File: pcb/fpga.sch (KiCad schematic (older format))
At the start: 29 parts, among them J1 CONN_INTEGRALSTICK_FPGA_DEVICE, Q1 SSM6N58NU, Q2 SSM6N58NU, Q3 SSM6N58NU, U12 DSC6001HI2A-025.0000‎, U2 XC7A50T-1FTG256C, U9 AT24MAC402-UDFN

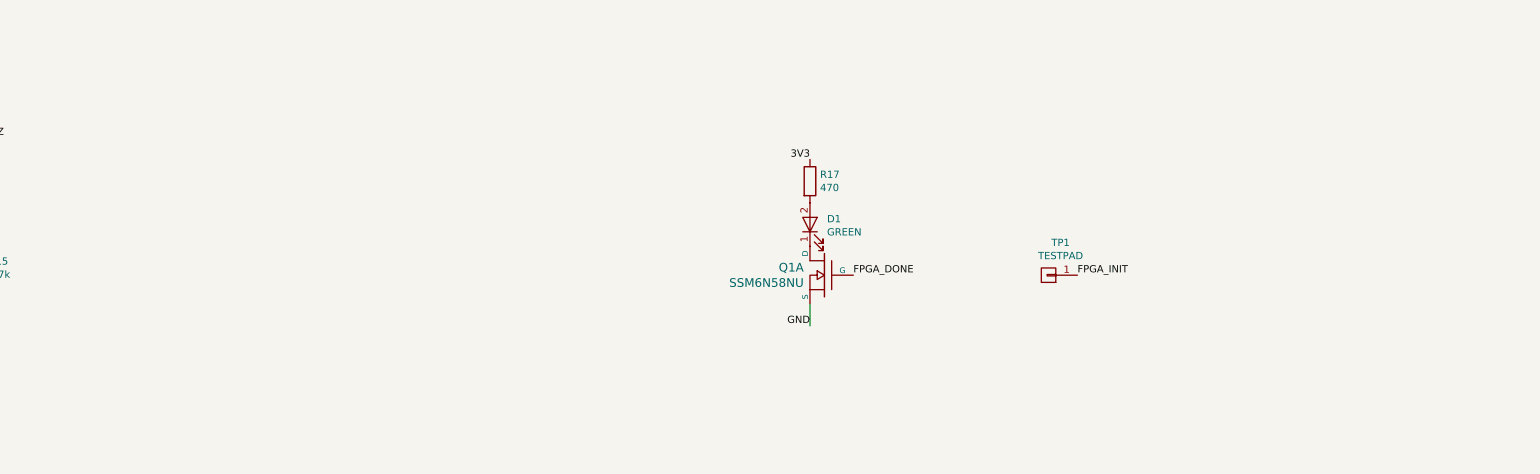
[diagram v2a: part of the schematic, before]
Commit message: Added layer-change caps by Q-strip
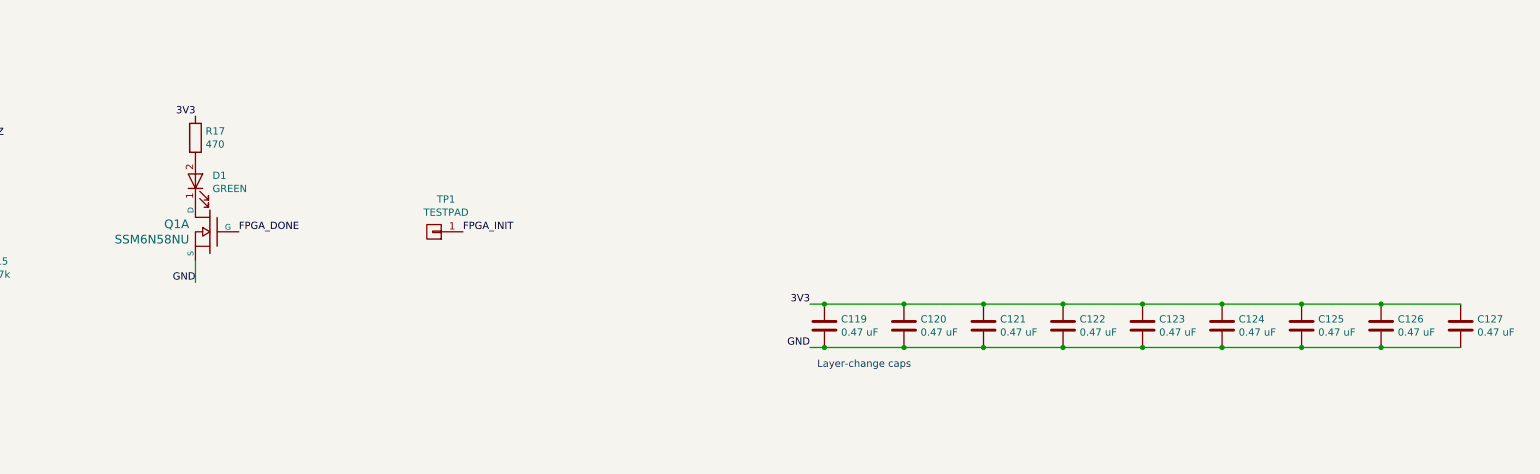
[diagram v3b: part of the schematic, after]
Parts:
- added C119, C120, C121, C122, C123, C124, C125, C126, C127: 0.47 uF, azonenberg_pcb:EIA_0402_CAP_NOSILK, symbol device:C
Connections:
- net 3V3: now also C119.1, C120.1, C121.1, C122.1, C123.1, C124.1, C125.1, C126.1, C127.1
- net GND: now also C119.2, C120.2, C121.2, C122.2, C123.2, C124.2, C125.2, C126.2, C127.2
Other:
- note added: "Layer-change caps"
- moved on the sheet: D1, Q1A, R17, TP1
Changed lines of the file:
@@
 Sheet 6 8
 Title "INTEGRALSTICK Compute Module"
-Date "2018-11-12"
+Date "2018-11-13"
 Rev "0.1"
 Comp "Andrew D. Zonenberg"
@@
 L special-azonenberg:SSM6N58NU_DUAL_NMOS Q1
 U 1 1 5BF27F1F
-P 11200 8050
-F 0 "Q1" H 11343 8103 60  0000 L CNN
-F 1 "SSM6N58NU" H 11343 7997 60  0000 L CNN
-F 2 "azonenberg_pcb:DFN_6_0.65MM_2x2MM_GDS" H 11200 8050 60  0001 C CNN
-F 3 "" H 11343 7944 60  0000 L CNN
-	1    11200 8050
+P 6950 7750
+F 0 "Q1" H 7093 7803 60  0000 L CNN
+F 1 "SSM6N58NU" H 7093 7697 60  0000 L CNN
+F 2 "azonenberg_pcb:DFN_6_0.65MM_2x2MM_GDS" H 6950 7750 60  0001 C CNN
+F 3 "" H 7093 7644 60  0000 L CNN
+	1    6950 7750
 	-1   0    0    -1
 $EndComp
@@
 L device:LED D1
 U 1 1 5BF295E2
-P 11100 7700
-F 0 "D1" V 11139 7582 50  0000 R CNN
-F 1 "GREEN" V 11048 7582 50  0000 R CNN
-F 2 "azonenberg_pcb:EIA_0603_LED" H 11100 7700 50  0001 C CNN
-F 3 "" H 11100 7700 50  0001 C CNN
-	1    11100 7700
+P 6850 7400
+F 0 "D1" V 6889 7282 50  0000 R CNN
+F 1 "GREEN" V 6798 7282 50  0000 R CNN
+F 2 "azonenberg_pcb:EIA_0603_LED" H 6850 7400 50  0001 C CNN
+F 3 "" H 6850 7400 50  0001 C CNN
+	1    6850 7400
 	0    -1   -1   0
 $EndComp
@@
 L device:R R17
 U 1 1 5BF2B413
-P 11100 7400
-F 0 "R17" H 11170 7446 50  0000 L CNN
-F 1 "470" H 11170 7355 50  0000 L CNN
-F 2 "azonenberg_pcb:EIA_0402_RES_NOSILK" V 11030 7400 50  0001 C CNN
-F 3 "" H 11100 7400 50  0001 C CNN
-	1    11100 7400
-	1    0    0    -1
-$EndComp
-Text Label 11100 7250 2    50   ~ 0
+P 6850 7100
+F 0 "R17" H 6920 7146 50  0000 L CNN
+F 1 "470" H 6920 7055 50  0000 L CNN
+F 2 "azonenberg_pcb:EIA_0402_RES_NOSILK" V 6780 7100 50  0001 C CNN
+F 3 "" H 6850 7100 50  0001 C CNN
+	1    6850 7100
+	1    0    0    -1
+$EndComp
+Text Label 6850 6950 2    50   ~ 0
 3V3
-Text Label 11100 8400 2    50   ~ 0
-GND
-Text Label 11400 8050 0    50   ~ 0
+Text Label 6850 8100 2    50   ~ 0
+GND
+Text Label 7150 7750 0    50   ~ 0
 FPGA_DONE
-Text Label 12950 8050 0    50   ~ 0
+Text Label 8700 7750 0    50   ~ 0
 FPGA_INIT
 Text Label 13750 5050 2    50   ~ 0
@@
 Connection ~ 12850 5050
 Wire Wire Line
-	11100 8250 11100 8400
+	6850 7950 6850 8100
 $Comp
 L conn:CONN_01X01 TP1
 U 1 1 5BF366F5
-P 12750 8050
-F 0 "TP1" H 12667 7825 50  0000 C CNN
-F 1 "TESTPAD" H 12667 7916 50  0000 C CNN
-F 2 "azonenberg_pcb:TESTPOINT_SMT_0.5MM" H 12750 8050 50  0001 C CNN
-F 3 "" H 12750 8050 50  0001 C CNN
-	1    12750 8050
+P 8500 7750
+F 0 "TP1" H 8417 7525 50  0000 C CNN
+F 1 "TESTPAD" H 8417 7616 50  0000 C CNN
+F 2 "azonenberg_pcb:TESTPOINT_SMT_0.5MM" H 8500 7750 50  0001 C CNN
+F 3 "" H 8500 7750 50  0001 C CNN
+	1    8500 7750
 	-1   0    0    1
 $EndComp
@@
 NoConn ~ 8400 4550
 NoConn ~ 8400 4450
+Text Notes 11150 8700 0    50   ~ 0
+Layer-change caps
+$Comp
+L device:C C?
+U 1 1 5BFC1C0D
+P 11200 8400
+AR Path="/5B6B7044/5BFC1C0D" Ref="C?"  Part="1"
+AR Path="/5B6B702C/5BFC1C0D" Ref="C119"  Part="1"
+F 0 "C119" H 11315 8446 50  0000 L CNN
+F 1 "0.47 uF" H 11315 8355 50  0000 L CNN
+F 2 "azonenberg_pcb:EIA_0402_CAP_NOSILK" H 11238 8250 50  0001 C CNN
+F 3 "" H 11200 8400 50  0001 C CNN
+	1    11200 8400
+	1    0    0    -1
+$EndComp
+Text Label 11100 8250 2    50   ~ 0
+3V3
+Text Label 11100 8550 2    50   ~ 0
+GND
+$Comp
+L device:C C?
+U 1 1 5BFC3321
+P 12300 8400
+AR Path="/5B6B7044/5BFC3321" Ref="C?"  Part="1"
+AR Path="/5B6B702C/5BFC3321" Ref="C121"  Part="1"
+F 0 "C121" H 12415 8446 50  0000 L CNN
+F 1 "0.47 uF" H 12415 8355 50  0000 L CNN
+F 2 "azonenberg_pcb:EIA_0402_CAP_NOSILK" H 12338 8250 50  0001 C CNN
+F 3 "" H 12300 8400 50  0001 C CNN
+	1    12300 8400
+	1    0    0    -1
+$EndComp
+$Comp
+L device:C C?
+U 1 1 5BFC390F
+P 12850 8400
+AR Path="/5B6B7044/5BFC390F" Ref="C?"  Part="1"
+AR Path="/5B6B702C/5BFC390F" Ref="C122"  Part="1"
+F 0 "C122" H 12965 8446 50  0000 L CNN
+F 1 "0.47 uF" H 12965 8355 50  0000 L CNN
+F 2 "azonenberg_pcb:EIA_0402_CAP_NOSILK" H 12888 8250 50  0001 C CNN
+F 3 "" H 12850 8400 50  0001 C CNN
+	1    12850 8400
+	1    0    0    -1
+$EndComp
+$Comp
+L device:C C?
+U 1 1 5BFC3D49
+P 13400 8400
+AR Path="/5B6B7044/5BFC3D49" Ref="C?"  Part="1"
+AR Path="/5B6B702C/5BFC3D49" Ref="C123"  Part="1"
+F 0 "C123" H 13515 8446 50  0000 L CNN
+F 1 "0.47 uF" H 13515 8355 50  0000 L CNN
+F 2 "azonenberg_pcb:EIA_0402_CAP_NOSILK" H 13438 8250 50  0001 C CNN
+F 3 "" H 13400 8400 50  0001 C CNN
+	1    13400 8400
+	1    0    0    -1
+$EndComp
+$Comp
+L device:C C?
+U 1 1 5BFC4329
+P 13950 8400
+AR Path="/5B6B7044/5BFC4329" Ref="C?"  Part="1"
+AR Path="/5B6B702C/5BFC4329" Ref="C124"  Part="1"
+F 0 "C124" H 14065 8446 50  0000 L CNN
+F 1 "0.47 uF" H 14065 8355 50  0000 L CNN
+F 2 "azonenberg_pcb:EIA_0402_CAP_NOSILK" H 13988 8250 50  0001 C CNN
+F 3 "" H 13950 8400 50  0001 C CNN
+	1    13950 8400
+	1    0    0    -1
+$EndComp
+$Comp
+L device:C C?
+U 1 1 5BFC4780
+P 14500 8400
+AR Path="/5B6B7044/5BFC4780" Ref="C?"  Part="1"
+AR Path="/5B6B702C/5BFC4780" Ref="C125"  Part="1"
+F 0 "C125" H 14615 8446 50  0000 L CNN
+F 1 "0.47 uF" H 14615 8355 50  0000 L CNN
+F 2 "azonenberg_pcb:EIA_0402_CAP_NOSILK" H 14538 8250 50  0001 C CNN
+F 3 "" H 14500 8400 50  0001 C CNN
+	1    14500 8400
+	1    0    0    -1
+$EndComp
+$Comp
+L device:C C?
+U 1 1 5BFC4BF1
+P 15050 8400
+AR Path="/5B6B7044/5BFC4BF1" Ref="C?"  Part="1"
+AR Path="/5B6B702C/5BFC4BF1" Ref="C126"  Part="1"
+F 0 "C126" H 15165 8446 50  0000 L CNN
+F 1 "0.47 uF" H 15165 8355 50  0000 L CNN
+F 2 "azonenberg_pcb:EIA_0402_CAP_NOSILK" H 15088 8250 50  0001 C CNN
+F 3 "" H 15050 8400 50  0001 C CNN
+	1    15050 8400
+	1    0    0    -1
+$EndComp
+$Comp
+L device:C C?
+U 1 1 5BFC52AC
+P 15600 8400
+AR Path="/5B6B7044/5BFC52AC" Ref="C?"  Part="1"
+AR Path="/5B6B702C/5BFC52AC" Ref="C127"  Part="1"
+F 0 "C127" H 15715 8446 50  0000 L CNN
+F 1 "0.47 uF" H 15715 8355 50  0000 L CNN
+F 2 "azonenberg_pcb:EIA_0402_CAP_NOSILK" H 15638 8250 50  0001 C CNN
+F 3 "" H 15600 8400 50  0001 C CNN
+	1    15600 8400
+	1    0    0    -1
+$EndComp
+$Comp
+L device:C C?
+U 1 1 5BFC6B38
+P 11750 8400
+AR Path="/5B6B7044/5BFC6B38" Ref="C?"  Part="1"
+AR Path="/5B6B702C/5BFC6B38" Ref="C120"  Part="1"
+F 0 "C120" H 11865 8446 50  0000 L CNN
+F 1 "0.47 uF" H 11865 8355 50  0000 L CNN
+F 2 "azonenberg_pcb:EIA_0402_CAP_NOSILK" H 11788 8250 50  0001 C CNN
+F 3 "" H 11750 8400 50  0001 C CNN
+	1    11750 8400
+	1    0    0    -1
+$EndComp
+Wire Wire Line
+	15600 8250 15050 8250
+Connection ~ 11200 8250
+Wire Wire Line
+	11200 8250 11100 8250
+Connection ~ 11750 8250
+Wire Wire Line
+	11750 8250 11200 8250
+Connection ~ 12300 8250
+Wire Wire Line
+	12300 8250 11750 8250
+Connection ~ 12850 8250
+Wire Wire Line
+	12850 8250 12300 8250
+Connection ~ 13400 8250
+Wire Wire Line
+	13400 8250 12850 8250
+Connection ~ 13950 8250
+Wire Wire Line
+	13950 8250 13400 8250
+Connection ~ 14500 8250
+Wire Wire Line
+	14500 8250 13950 8250
+Connection ~ 15050 8250
+Wire Wire Line
+	15050 8250 14500 8250
+Wire Wire Line
+	11100 8550 11200 8550
+Connection ~ 11200 8550
+Wire Wire Line
+	11200 8550 11750 8550
+Connection ~ 11750 8550
+Wire Wire Line
+	11750 8550 12300 8550
+Connection ~ 12300 8550
+Wire Wire Line
+	12300 8550 12850 8550
+Connection ~ 12850 8550
+Wire Wire Line
+	12850 8550 13400 8550
+Connection ~ 13400 8550
+Wire Wire Line
+	13400 8550 13950 8550
+Connection ~ 13950 8550
+Wire Wire Line
+	13950 8550 14500 8550
+Connection ~ 14500 8550
+Wire Wire Line
+	14500 8550 15050 8550
+Connection ~ 15050 8550
+Wire Wire Line
+	15050 8550 15600 8550
 $EndSCHEMATC

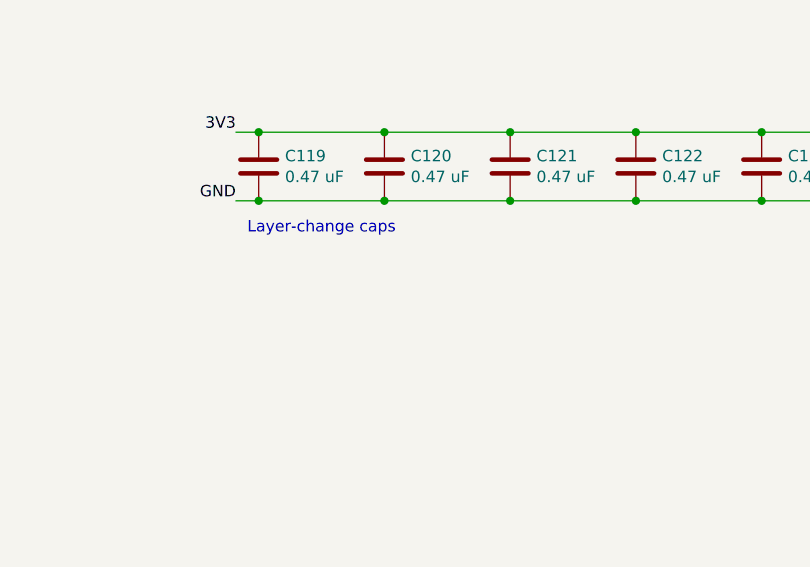
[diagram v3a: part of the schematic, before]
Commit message: Initial FPGA plane layout
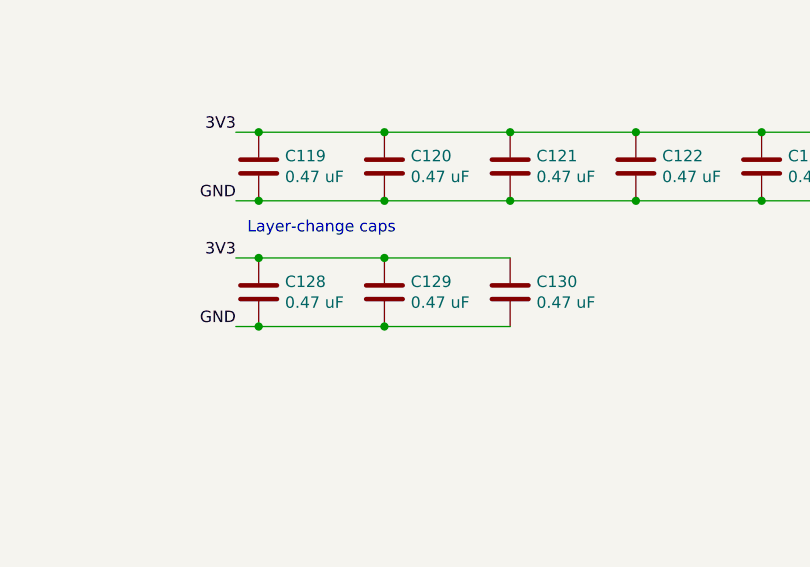
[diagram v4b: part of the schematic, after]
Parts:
- added C128, C129, C130: 0.47 uF, azonenberg_pcb:EIA_0402_CAP_NOSILK, symbol device:C
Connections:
- net 3V3: now also C128.1, C129.1, C130.1
- net GND: now also C128.2, C129.2, C130.2
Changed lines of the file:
@@
 Wire Wire Line
 	15050 8550 15600 8550
+$Comp
+L device:C C?
+U 1 1 5BFD0553
+P 11200 8950
+AR Path="/5B6B7044/5BFD0553" Ref="C?"  Part="1"
+AR Path="/5B6B702C/5BFD0553" Ref="C128"  Part="1"
+F 0 "C128" H 11315 8996 50  0000 L CNN
+F 1 "0.47 uF" H 11315 8905 50  0000 L CNN
+F 2 "azonenberg_pcb:EIA_0402_CAP_NOSILK" H 11238 8800 50  0001 C CNN
+F 3 "" H 11200 8950 50  0001 C CNN
+	1    11200 8950
+	1    0    0    -1
+$EndComp
+Text Label 11100 8800 2    50   ~ 0
+3V3
+Text Label 11100 9100 2    50   ~ 0
+GND
+Wire Wire Line
+	11100 9100 11200 9100
+Wire Wire Line
+	11200 8800 11100 8800
+$Comp
+L device:C C?
+U 1 1 5BFD65D8
+P 11750 8950
+AR Path="/5B6B7044/5BFD65D8" Ref="C?"  Part="1"
+AR Path="/5B6B702C/5BFD65D8" Ref="C129"  Part="1"
+F 0 "C129" H 11865 8996 50  0000 L CNN
+F 1 "0.47 uF" H 11865 8905 50  0000 L CNN
+F 2 "azonenberg_pcb:EIA_0402_CAP_NOSILK" H 11788 8800 50  0001 C CNN
+F 3 "" H 11750 8950 50  0001 C CNN
+	1    11750 8950
+	1    0    0    -1
+$EndComp
+Wire Wire Line
+	11750 8800 11200 8800
+Connection ~ 11200 8800
+Wire Wire Line
+	11750 9100 11200 9100
+Connection ~ 11200 9100
+$Comp
+L device:C C?
+U 1 1 5BFDC11E
+P 12300 8950
+AR Path="/5B6B7044/5BFDC11E" Ref="C?"  Part="1"
+AR Path="/5B6B702C/5BFDC11E" Ref="C130"  Part="1"
+F 0 "C130" H 12415 8996 50  0000 L CNN
+F 1 "0.47 uF" H 12415 8905 50  0000 L CNN
+F 2 "azonenberg_pcb:EIA_0402_CAP_NOSILK" H 12338 8800 50  0001 C CNN
+F 3 "" H 12300 8950 50  0001 C CNN
+	1    12300 8950
+	1    0    0    -1
+$EndComp
+Wire Wire Line
+	12300 8800 11750 8800
+Connection ~ 11750 8800
+Wire Wire Line
+	12300 9100 11750 9100
+Connection ~ 11750 9100
 $EndSCHEMATC

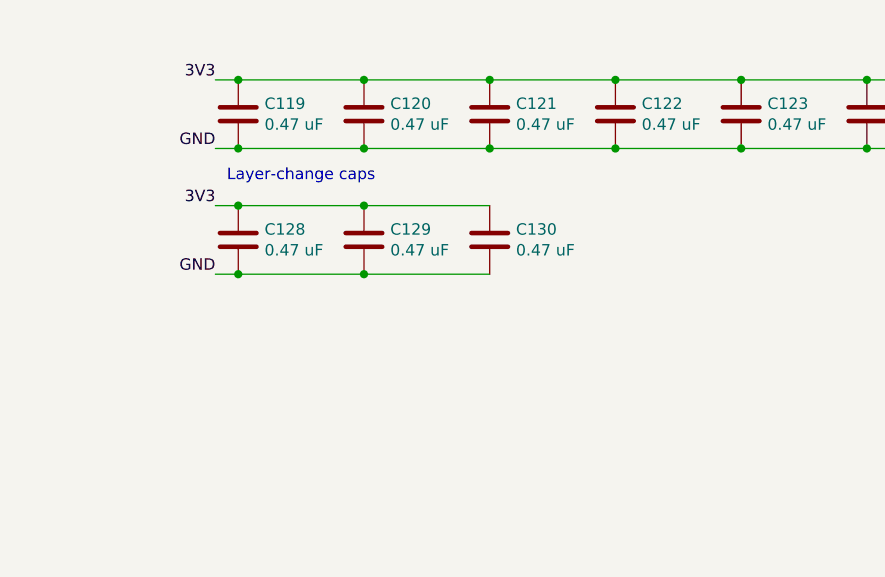
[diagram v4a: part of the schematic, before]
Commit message: Initial routing of LVCMOS18 GPIO bus. Hooked up a few 0603 decoupling caps.
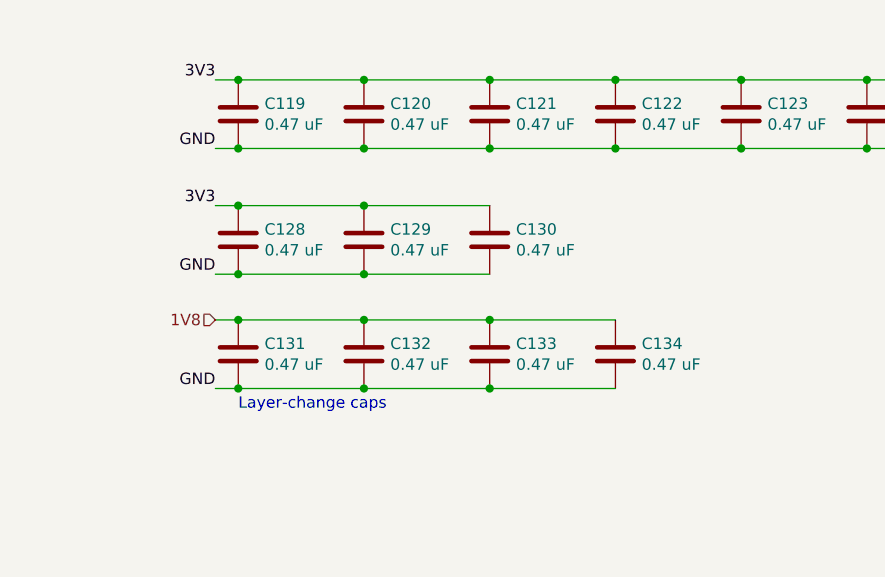
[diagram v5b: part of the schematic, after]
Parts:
- added C131, C132, C133, C134: 0.47 uF, azonenberg_pcb:EIA_0402_CAP_NOSILK, symbol device:C
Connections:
- net GND: now also C131.2, C132.2, C133.2, C134.2
- new net 1V8: C131.1, C132.1, C133.1, C134.1
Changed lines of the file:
@@
 NoConn ~ 8400 4550
 NoConn ~ 8400 4450
-Text Notes 11150 8700 0    50   ~ 0
+Text Notes 11200 9700 0    50   ~ 0
 Layer-change caps
 $Comp
@@
 	12300 9100 11750 9100
 Connection ~ 11750 9100
+$Comp
+L device:C C?
+U 1 1 5C091EF9
+P 11200 9450
+AR Path="/5B6B7044/5C091EF9" Ref="C?"  Part="1"
+AR Path="/5B6B702C/5C091EF9" Ref="C131"  Part="1"
+F 0 "C131" H 11315 9496 50  0000 L CNN
+F 1 "0.47 uF" H 11315 9405 50  0000 L CNN
+F 2 "azonenberg_pcb:EIA_0402_CAP_NOSILK" H 11238 9300 50  0001 C CNN
+F 3 "" H 11200 9450 50  0001 C CNN
+	1    11200 9450
+	1    0    0    -1
+$EndComp
+Text Label 11100 9600 2    50   ~ 0
+GND
+Wire Wire Line
+	11100 9600 11200 9600
+Wire Wire Line
+	11200 9300 11100 9300
+$Comp
+L device:C C?
+U 1 1 5C091F07
+P 11750 9450
+AR Path="/5B6B7044/5C091F07" Ref="C?"  Part="1"
+AR Path="/5B6B702C/5C091F07" Ref="C132"  Part="1"
+F 0 "C132" H 11865 9496 50  0000 L CNN
+F 1 "0.47 uF" H 11865 9405 50  0000 L CNN
+F 2 "azonenberg_pcb:EIA_0402_CAP_NOSILK" H 11788 9300 50  0001 C CNN
+F 3 "" H 11750 9450 50  0001 C CNN
+	1    11750 9450
+	1    0    0    -1
+$EndComp
+Wire Wire Line
+	11750 9300 11200 9300
+Connection ~ 11200 9300
+Wire Wire Line
+	11750 9600 11200 9600
+Connection ~ 11200 9600
+$Comp
+L device:C C?
+U 1 1 5C091F15
+P 12300 9450
+AR Path="/5B6B7044/5C091F15" Ref="C?"  Part="1"
+AR Path="/5B6B702C/5C091F15" Ref="C133"  Part="1"
+F 0 "C133" H 12415 9496 50  0000 L CNN
+F 1 "0.47 uF" H 12415 9405 50  0000 L CNN
+F 2 "azonenberg_pcb:EIA_0402_CAP_NOSILK" H 12338 9300 50  0001 C CNN
+F 3 "" H 12300 9450 50  0001 C CNN
+	1    12300 9450
+	1    0    0    -1
+$EndComp
+Wire Wire Line
+	12300 9300 11750 9300
+Connection ~ 11750 9300
+Wire Wire Line
+	12300 9600 11750 9600
+Connection ~ 11750 9600
+$Comp
+L device:C C?
+U 1 1 5C094F88
+P 12850 9450
+AR Path="/5B6B7044/5C094F88" Ref="C?"  Part="1"
+AR Path="/5B6B702C/5C094F88" Ref="C134"  Part="1"
+F 0 "C134" H 12965 9496 50  0000 L CNN
+F 1 "0.47 uF" H 12965 9405 50  0000 L CNN
+F 2 "azonenberg_pcb:EIA_0402_CAP_NOSILK" H 12888 9300 50  0001 C CNN
+F 3 "" H 12850 9450 50  0001 C CNN
+	1    12850 9450
+	1    0    0    -1
+$EndComp
+Wire Wire Line
+	12850 9300 12300 9300
+Connection ~ 12300 9300
+Wire Wire Line
+	12850 9600 12300 9600
+Connection ~ 12300 9600
+Text HLabel 11100 9300 0    50   Input ~ 0
+1V8
 $EndSCHEMATC
